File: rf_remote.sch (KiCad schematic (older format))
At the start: 15 parts, among them P1 CONN_01X04, P2 CONN_01X01, U1 SAMD21E18, U2 RFM69CW-915MHZ

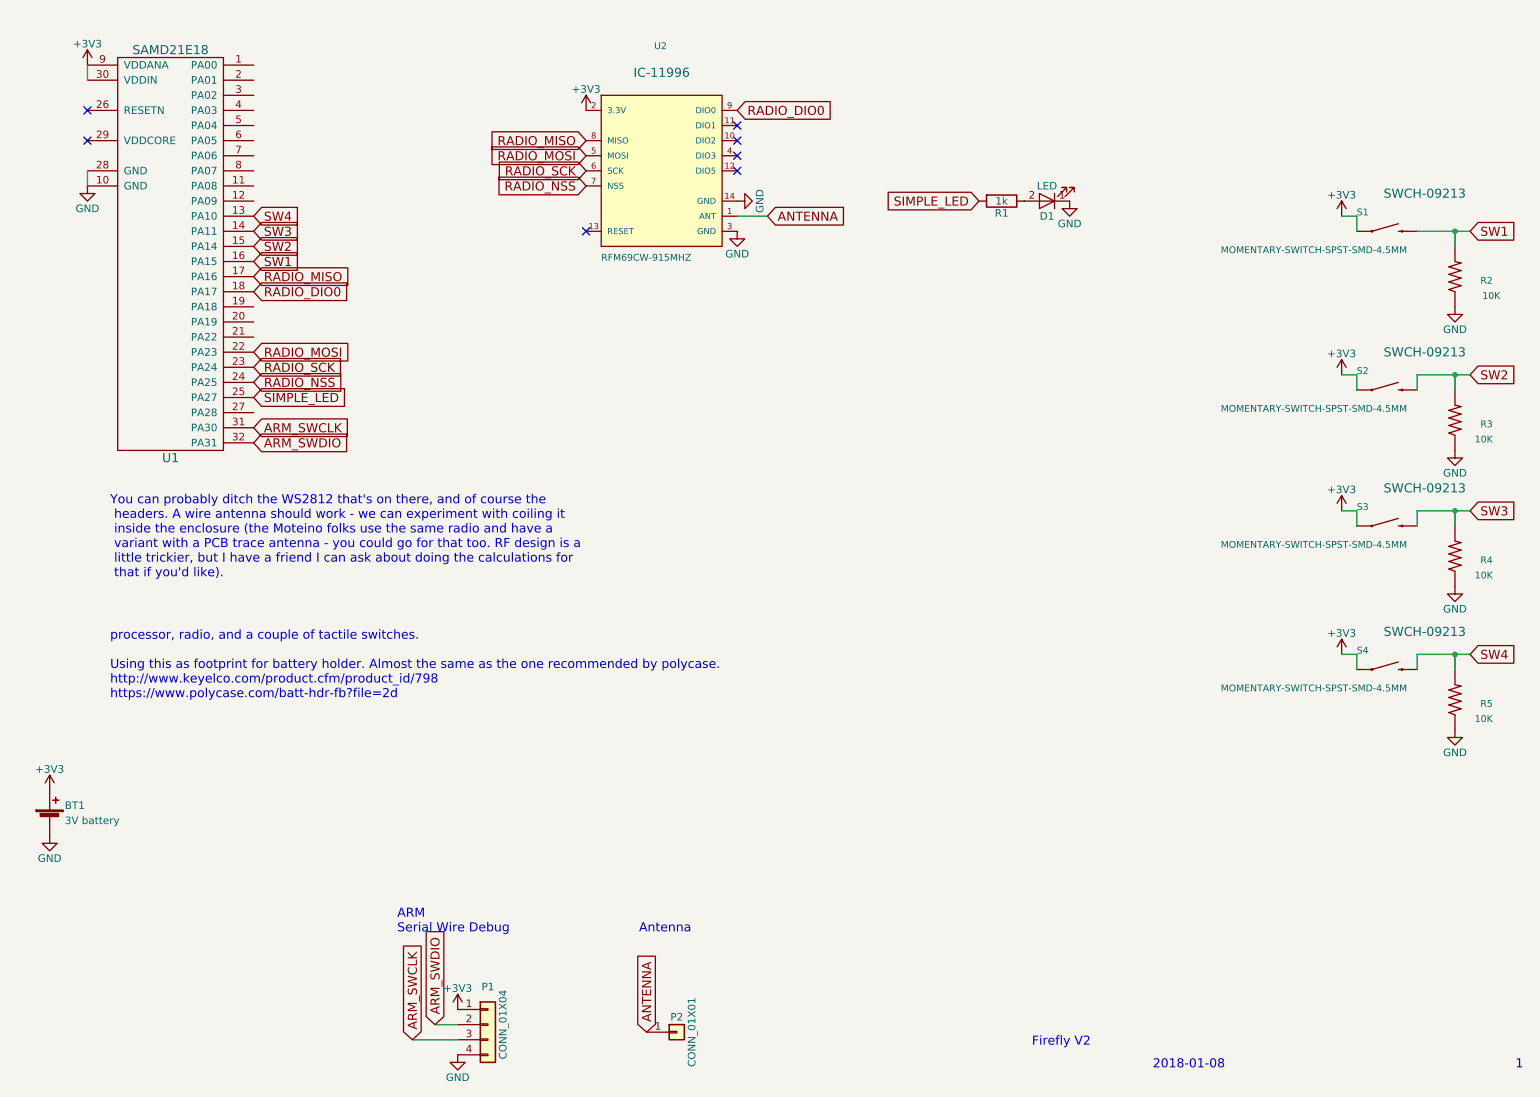
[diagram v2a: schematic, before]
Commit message: removed pulldowns
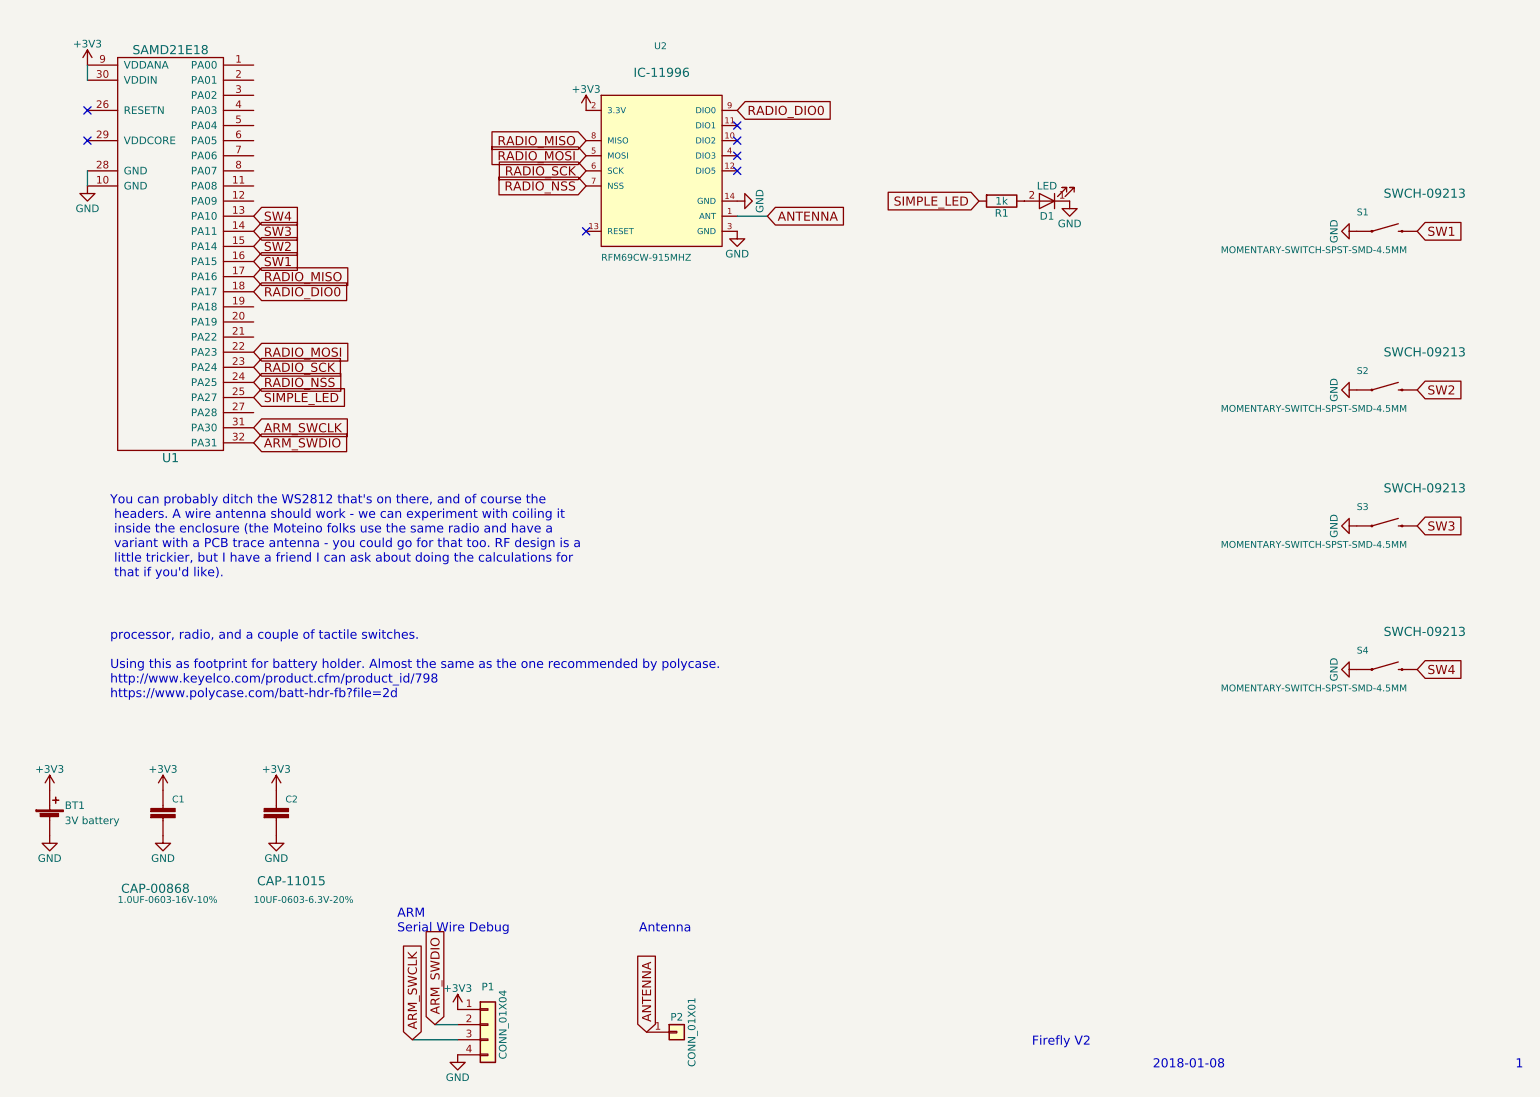
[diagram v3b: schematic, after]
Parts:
- removed R2, R3, R4, R5: 10K, Resistors_SMD:R_0603_HandSoldering, symbol RESISTOR0603
- added C1: 1.0UF-0603-16V-10%, Capacitors_SMD:C_0603, symbol 1.0UF-0603-16V-10%
- added C2: 10UF-0603-6.3V-20%, Capacitors_SMD:C_0603, symbol 10UF-0603-6.3V-20%
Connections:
- net +3V3: now also C1.1, C2.1; no longer S1.2 (1), S1.3 (1), S2.2 (1), S2.3 (1), S3.2 (1), S3.3 (1), S4.2 (1), S4.3 (1)
- net GND: now also S1.2 (1), S1.3 (1), S2.2 (1), S2.3 (1), S3.2 (1), S3.3 (1), S4.2 (1), S4.3 (1), C1.2, C2.2
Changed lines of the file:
@@
 Text GLabel 2200 2300 2    60   Input ~ 0
 SW1
-Text GLabel 10250 2100 2    60   Input ~ 0
+Text GLabel 9900 2100 2    60   Input ~ 0
 SW1
 Text GLabel 2200 2200 2    60   Input ~ 0
@@
 Text GLabel 2200 2000 2    60   Input ~ 0
 SW4
-Text GLabel 10250 3050 2    60   Input ~ 0
+Text GLabel 9900 3150 2    60   Input ~ 0
 SW2
-Text GLabel 10250 3950 2    60   Input ~ 0
+Text GLabel 9900 4050 2    60   Input ~ 0
 SW3
-Text GLabel 10250 4900 2    60   Input ~ 0
+Text GLabel 9900 5000 2    60   Input ~ 0
 SW4
 $Comp
 L GND #PWR09
 U 1 1 5ADD2C56
-P 10150 2600
-F 0 "#PWR09" H 10150 2350 50  0001 C CNN
-F 1 "GND" H 10150 2450 50  0000 C CNN
-F 2 "" H 10150 2600 50  0001 C CNN
-F 3 "" H 10150 2600 50  0001 C CNN
-	1    10150 2600
-	1    0    0    -1
-$EndComp
-Wire Wire Line
-	9900 2100 10250 2100
-Wire Wire Line
-	10150 2100 10150 2200
-Connection ~ 10150 2100
-Wire Wire Line
-	10250 3050 9900 3050
-Wire Wire Line
-	10150 3150 10150 3050
-Connection ~ 10150 3050
-Wire Wire Line
-	9900 3050 9900 3150
-Wire Wire Line
-	9500 3150 9500 3050
-Wire Wire Line
-	9500 2100 9500 2000
-Wire Wire Line
-	9500 4050 9500 3950
-Wire Wire Line
-	9500 5000 9500 4900
-Wire Wire Line
-	9900 5000 9900 4900
-Wire Wire Line
-	9900 4050 9900 3950
-Wire Wire Line
-	9900 3950 10250 3950
-Wire Wire Line
-	10150 3950 10150 4050
-Connection ~ 10150 3950
-Wire Wire Line
-	10150 5000 10150 4900
-Wire Wire Line
-	9900 4900 10250 4900
-Connection ~ 10150 4900
-$Comp
-L +3V3 #PWR010
-U 1 1 5ADD30DC
-P 9400 2000
-F 0 "#PWR010" H 9400 1850 50  0001 C CNN
-F 1 "+3V3" H 9400 2140 50  0000 C CNN
-F 2 "" H 9400 2000 50  0001 C CNN
-F 3 "" H 9400 2000 50  0001 C CNN
-	1    9400 2000
-	1    0    0    -1
-$EndComp
-$Comp
-L +3V3 #PWR011
-U 1 1 5ADD3146
-P 9400 3050
-F 0 "#PWR011" H 9400 2900 50  0001 C CNN
-F 1 "+3V3" H 9400 3190 50  0000 C CNN
-F 2 "" H 9400 3050 50  0001 C CNN
-F 3 "" H 9400 3050 50  0001 C CNN
-	1    9400 3050
-	1    0    0    -1
-$EndComp
-$Comp
-L +3V3 #PWR012
-U 1 1 5ADD318A
-P 9400 3950
-F 0 "#PWR012" H 9400 3800 50  0001 C CNN
-F 1 "+3V3" H 9400 4090 50  0000 C CNN
-F 2 "" H 9400 3950 50  0001 C CNN
-F 3 "" H 9400 3950 50  0001 C CNN
-	1    9400 3950
-	1    0    0    -1
-$EndComp
-$Comp
-L +3V3 #PWR013
-U 1 1 5ADD31CE
-P 9400 4900
-F 0 "#PWR013" H 9400 4750 50  0001 C CNN
-F 1 "+3V3" H 9400 5040 50  0000 C CNN
-F 2 "" H 9400 4900 50  0001 C CNN
-F 3 "" H 9400 4900 50  0001 C CNN
-	1    9400 4900
-	1    0    0    -1
-$EndComp
-Wire Wire Line
-	9500 2000 9400 2000
-Wire Wire Line
-	9500 3050 9400 3050
-Wire Wire Line
-	9500 3950 9400 3950
-Wire Wire Line
-	9500 4900 9400 4900
-$Comp
-L RESISTOR0603 R2
-U 1 1 5ADD3945
-P 10150 2400
-F 0 "R2" V 10150 2150 45  0000 L BNN
-F 1 "10K " V 10050 2100 45  0000 L BNN
-F 2 "Resistors_SMD:R_0603_HandSoldering" H 10150 2550 20  0001 C CNN
-F 3 "" H 10150 2400 60  0001 C CNN
-F 4 " " H 10150 2600 60  0000 C CNN "Field4"
-	1    10150 2400
-	0    -1   -1   0
+P 9500 2100
+F 0 "#PWR09" H 9500 1850 50  0001 C CNN
+F 1 "GND" H 9500 1950 50  0000 C CNN
+F 2 "" H 9500 2100 50  0001 C CNN
+F 3 "" H 9500 2100 50  0001 C CNN
+	1    9500 2100
+	0    1    1    0
 $EndComp
 $Comp
 L GND #PWR014
 U 1 1 5ADD4016
-P 10150 3550
-F 0 "#PWR014" H 10150 3300 50  0001 C CNN
-F 1 "GND" H 10150 3400 50  0000 C CNN
-F 2 "" H 10150 3550 50  0001 C CNN
-F 3 "" H 10150 3550 50  0001 C CNN
-	1    10150 3550
-	1    0    0    -1
-$EndComp
-$Comp
-L RESISTOR0603 R3
-U 1 1 5ADD401D
-P 10150 3350
-F 0 "R3" V 10150 3100 45  0000 L BNN
-F 1 "10K" V 10050 3100 45  0000 L BNN
-F 2 "Resistors_SMD:R_0603_HandSoldering" H 10150 3500 20  0001 C CNN
-F 3 "" H 10150 3350 60  0001 C CNN
-F 4 " " H 10150 3550 60  0000 C CNN "Field4"
-	1    10150 3350
-	0    -1   -1   0
+P 9500 3150
+F 0 "#PWR014" H 9500 2900 50  0001 C CNN
+F 1 "GND" H 9500 3000 50  0000 C CNN
+F 2 "" H 9500 3150 50  0001 C CNN
+F 3 "" H 9500 3150 50  0001 C CNN
+	1    9500 3150
+	0    1    1    0
 $EndComp
 $Comp
 L GND #PWR015
 U 1 1 5ADD418C
-P 10150 4450
-F 0 "#PWR015" H 10150 4200 50  0001 C CNN
-F 1 "GND" H 10150 4300 50  0000 C CNN
-F 2 "" H 10150 4450 50  0001 C CNN
-F 3 "" H 10150 4450 50  0001 C CNN
-	1    10150 4450
-	1    0    0    -1
-$EndComp
-$Comp
-L RESISTOR0603 R4
-U 1 1 5ADD4193
-P 10150 4250
-F 0 "R4" V 10150 4000 45  0000 L BNN
-F 1 "10K" V 10050 4000 45  0000 L BNN
-F 2 "Resistors_SMD:R_0603_HandSoldering" H 10150 4400 20  0001 C CNN
-F 3 "" H 10150 4250 60  0001 C CNN
-F 4 " " H 10150 4450 60  0000 C CNN "Field4"
-	1    10150 4250
-	0    -1   -1   0
+P 9500 4050
+F 0 "#PWR015" H 9500 3800 50  0001 C CNN
+F 1 "GND" H 9500 3900 50  0000 C CNN
+F 2 "" H 9500 4050 50  0001 C CNN
+F 3 "" H 9500 4050 50  0001 C CNN
+	1    9500 4050
+	0    1    1    0
 $EndComp
 $Comp
 L GND #PWR016
 U 1 1 5ADD4235
-P 10150 5400
-F 0 "#PWR016" H 10150 5150 50  0001 C CNN
-F 1 "GND" H 10150 5250 50  0000 C CNN
-F 2 "" H 10150 5400 50  0001 C CNN
-F 3 "" H 10150 5400 50  0001 C CNN
-	1    10150 5400
-	1    0    0    -1
-$EndComp
-$Comp
-L RESISTOR0603 R5
-U 1 1 5ADD423C
-P 10150 5200
-F 0 "R5" V 10150 4950 45  0000 L BNN
-F 1 "10K" V 10050 4950 45  0000 L BNN
-F 2 "Resistors_SMD:R_0603_HandSoldering" H 10150 5350 20  0001 C CNN
-F 3 "" H 10150 5200 60  0001 C CNN
-F 4 " " H 10150 5400 60  0000 C CNN "Field4"
-	1    10150 5200
-	0    -1   -1   0
+P 9500 5000
+F 0 "#PWR016" H 9500 4750 50  0001 C CNN
+F 1 "GND" H 9500 4850 50  0000 C CNN
+F 2 "" H 9500 5000 50  0001 C CNN
+F 3 "" H 9500 5000 50  0001 C CNN
+	1    9500 5000
+	0    1    1    0
 $EndComp
 $Comp
@@
 	1    0    0    -1
 $EndComp
+$Comp
+L 1.0UF-0603-16V-10% C1
+U 1 1 5B25ACEC
+P 1600 6000
+F 0 "C1" H 1660 6115 45  0000 L BNN
+F 1 "1.0UF-0603-16V-10%" H 1300 5450 45  0000 L BNN
+F 2 "Capacitors_SMD:C_0603" H 1600 6250 20  0001 C CNN
+F 3 "" H 1600 6000 50  0001 C CNN
+F 4 "CAP-00868" H 1550 5550 60  0000 C CNN "Field4"
+	1    1600 6000
+	1    0    0    -1
+$EndComp
+$Comp
+L 10UF-0603-6.3V-20% C2
+U 1 1 5B25AEA2
+P 2350 6000
+F 0 "C2" H 2410 6115 45  0000 L BNN
+F 1 "10UF-0603-6.3V-20%" H 2200 5450 45  0000 L BNN
+F 2 "Capacitors_SMD:C_0603" H 2350 6250 20  0001 C CNN
+F 3 "" H 2350 6000 50  0001 C CNN
+F 4 "CAP-11015" H 2450 5600 60  0000 C CNN "Field4"
+	1    2350 6000
+	1    0    0    -1
+$EndComp
+$Comp
+L +3V3 #PWR019
+U 1 1 5B25B2B9
+P 1600 5800
+F 0 "#PWR019" H 1600 5650 50  0001 C CNN
+F 1 "+3V3" H 1600 5940 50  0000 C CNN
+F 2 "" H 1600 5800 50  0001 C CNN
+F 3 "" H 1600 5800 50  0001 C CNN
+	1    1600 5800
+	1    0    0    -1
+$EndComp
+$Comp
+L +3V3 #PWR020
+U 1 1 5B25B308
+P 2350 5800
+F 0 "#PWR020" H 2350 5650 50  0001 C CNN
+F 1 "+3V3" H 2350 5940 50  0000 C CNN
+F 2 "" H 2350 5800 50  0001 C CNN
+F 3 "" H 2350 5800 50  0001 C CNN
+	1    2350 5800
+	1    0    0    -1
+$EndComp
+$Comp
+L GND #PWR021
+U 1 1 5B25B346
+P 1600 6100
+F 0 "#PWR021" H 1600 5850 50  0001 C CNN
+F 1 "GND" H 1600 5950 50  0000 C CNN
+F 2 "" H 1600 6100 50  0001 C CNN
+F 3 "" H 1600 6100 50  0001 C CNN
+	1    1600 6100
+	1    0    0    -1
+$EndComp
+$Comp
+L GND #PWR022
+U 1 1 5B25B384
+P 2350 6100
+F 0 "#PWR022" H 2350 5850 50  0001 C CNN
+F 1 "GND" H 2350 5950 50  0000 C CNN
+F 2 "" H 2350 6100 50  0001 C CNN
+F 3 "" H 2350 6100 50  0001 C CNN
+	1    2350 6100
+	1    0    0    -1
+$EndComp
